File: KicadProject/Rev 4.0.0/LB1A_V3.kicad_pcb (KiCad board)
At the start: 6 copper layers, 42 x 42 mm, 187 parts, among them J601 2337019-1, J602 2337019-1, U101 STM32MP157CAA3, U201 AS4C256M16D3LC-12BCN, U401 STPMIC1xPQR, U501 S40FC004C1B2C00000, U601 LBEE59B1LV-278, U701 DF40C-70DP-0.4V(51), U702 DF40C-100DP-0.4V(51), U703 DF40C-100DP-0.4V(51), X101 32.768kHz, Y101 24MHz

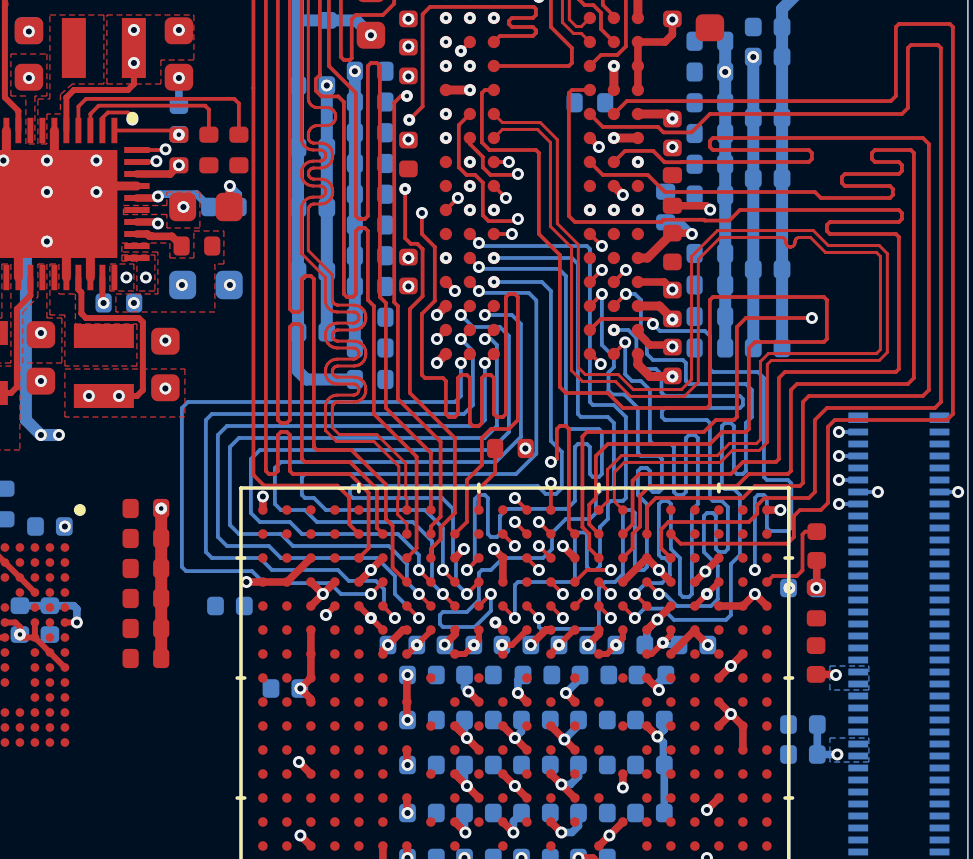
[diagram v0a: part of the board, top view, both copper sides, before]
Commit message: cleaning traces on L6 and rerouting
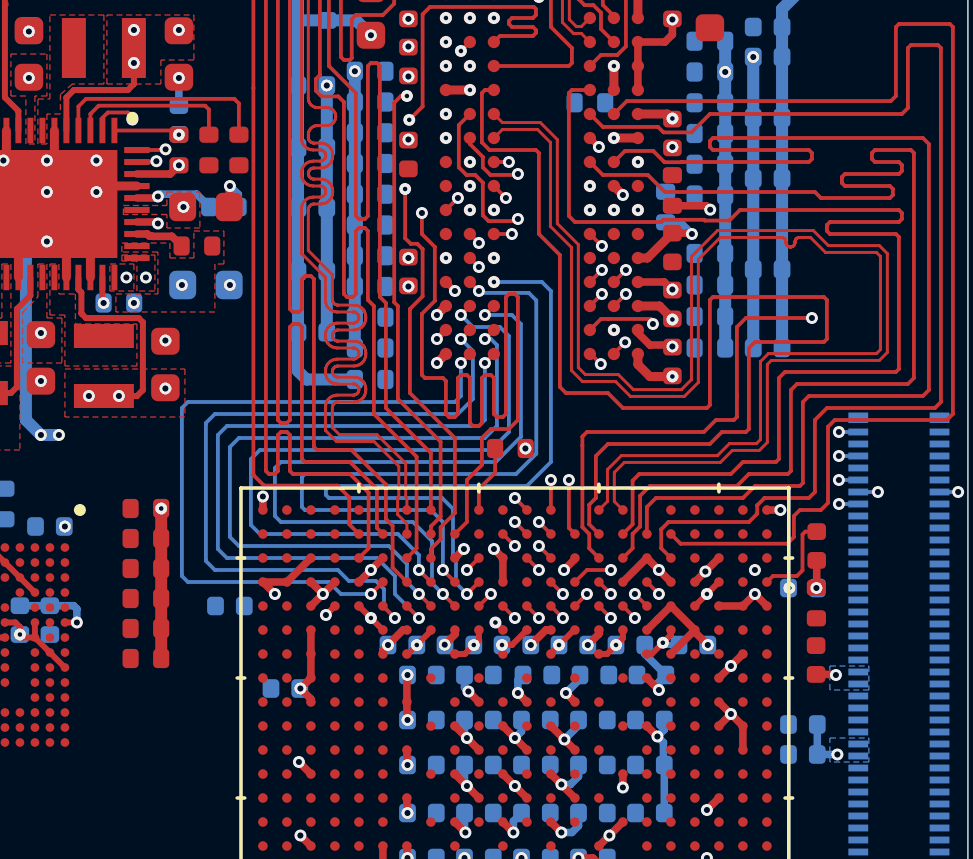
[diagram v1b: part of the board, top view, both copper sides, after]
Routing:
- net /MPU_DDR3L_Memory/DDR_BA2: track 23.5 -> 0.57 mm
- net /MPU_DDR3L_Memory/DDR_A6: track 23.4 -> 0.57 mm
- net /MPU_DDR3L_Memory/DDR_CSN: track 23.6 -> 0.99 mm
- net /MPU_DDR3L_Memory/DDR_BA0: track 23.5 -> 0.99 mm
- net /MPU_DDR3L_Memory/DDR_A4: track 23.6 -> 1.13 mm
- net /MPU_DDR3L_Memory/DDR_A1: track 23.5 -> 1.13 mm
- net /MPU_DDR3L_Memory/DDR_BA1: track 23.5 -> 1.13 mm
- net /MPU_DDR3L_Memory/DDR_A14: track 23.4 -> 1.07 mm
- net /MPU_DDR3L_Memory/DDR_A8: track 23.4 -> 1.11 mm
- net /MPU_DDR3L_Memory/DDR_A11: track 25.9 -> 10.3 mm
- net GND: track 203.9 -> 205.4 mm, vias 163 -> 162
- net /MPU_DDR3L_Memory/DDR_CLK_P: vias 1 -> 2

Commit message: some more changes
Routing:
- net /MPU_DDR3L_Memory/DDR_CLK_N: track 0.57 -> 32.7 mm
- net /MPU_DDR3L_Memory/DDR_CLK_P: track 0.57 -> 32.7 mm
- net /MPU_DDR3L_Memory/DDR_A11: track 10.3 -> 3.79 mm, vias 3 -> 2

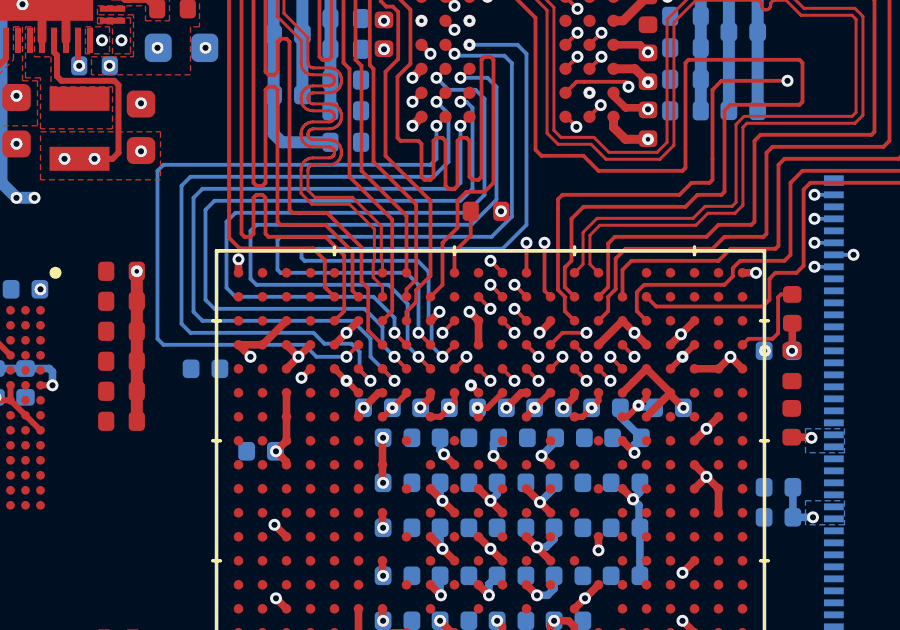
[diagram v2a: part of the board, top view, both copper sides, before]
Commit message: adjusted ground via
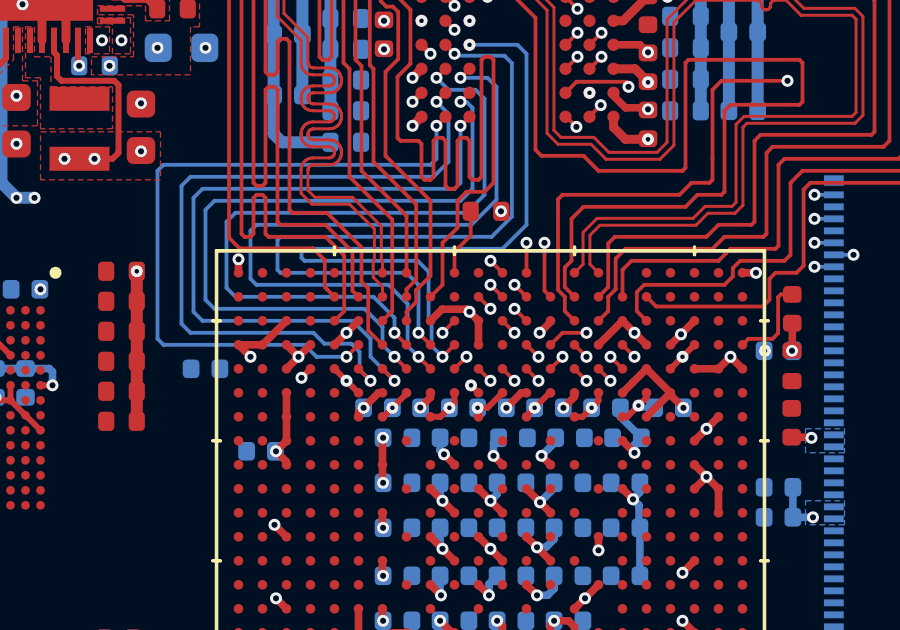
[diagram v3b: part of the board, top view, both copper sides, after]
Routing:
- net GND: track 205.4 -> 206.4 mm, vias 162 -> 161
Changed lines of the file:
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@@
     (thickness 1.2)
     (drawings 8)
-    (tracks 2430)
+    (tracks 2431)
     (zones 0)
     (modules 187)
@@
     (0 L1_Sig_Pwr.Cu mixed hide)
     (1 L2_Gnd.Cu power hide)
-    (2 L3_Sig_Pwr.Cu mixed)
-    (3 L4_Sig_Gnd.Cu mixed)
+    (2 L3_Sig_Pwr.Cu mixed hide)
+    (3 L4_Sig_Gnd.Cu mixed hide)
     (4 L5_Gnd_Pwr.Cu power hide)
     (31 L6_Sig_Pwr.Cu mixed)
@@
   (segment (start 204.280677 97.26) (end 204.41 97.389323) (width 0.254) (layer L1_Sig_Pwr.Cu) (net 1))
   (segment (start 203.15 97.26) (end 204.280677 97.26) (width 0.254) (layer L1_Sig_Pwr.Cu) (net 1))
-  (via (at 196.2 108.7) (size 0.4) (drill 0.2) (layers L1_Sig_Pwr.Cu L6_Sig_Pwr.Cu) (net 1))
-  (segment (start 195.9 109) (end 196.2 108.7) (width 0.254) (layer L1_Sig_Pwr.Cu) (net 1))
-  (segment (start 195.9 109.000001) (end 195.9 109) (width 0.254) (layer L1_Sig_Pwr.Cu) (net 1))
   (via (at 197.2 108.7) (size 0.4) (drill 0.2) (layers L1_Sig_Pwr.Cu L6_Sig_Pwr.Cu) (net 1))
   (segment (start 197.5 109) (end 197.2 108.7) (width 0.254) (layer L1_Sig_Pwr.Cu) (net 1))
@@
   (via (at 189.9 110.2) (size 0.4) (drill 0.2) (layers L1_Sig_Pwr.Cu L6_Sig_Pwr.Cu) (net 1))
   (segment (start 189.500001 109.800001) (end 189.9 110.2) (width 0.254) (layer L1_Sig_Pwr.Cu) (net 1))
+  (segment (start 197.113 108.613) (end 197.2 108.7) (width 0.254) (layer L1_Sig_Pwr.Cu) (net 1))
+  (segment (start 196.287 108.613) (end 197.113 108.613) (width 0.254) (layer L1_Sig_Pwr.Cu) (net 1))
+  (segment (start 195.9 109) (end 196.287 108.613) (width 0.254) (layer L1_Sig_Pwr.Cu) (net 1))
+  (segment (start 195.9 109.000001) (end 195.9 109) (width 0.254) (layer L1_Sig_Pwr.Cu) (net 1))
   (via (at 186.7 94.89) (size 0.4) (drill 0.15) (layers L1_Sig_Pwr.Cu L6_Sig_Pwr.Cu) (net 2))
   (segment (start 186.56 94.75) (end 186.7 94.89) (width 0.127) (layer L1_Sig_Pwr.Cu) (net 2))

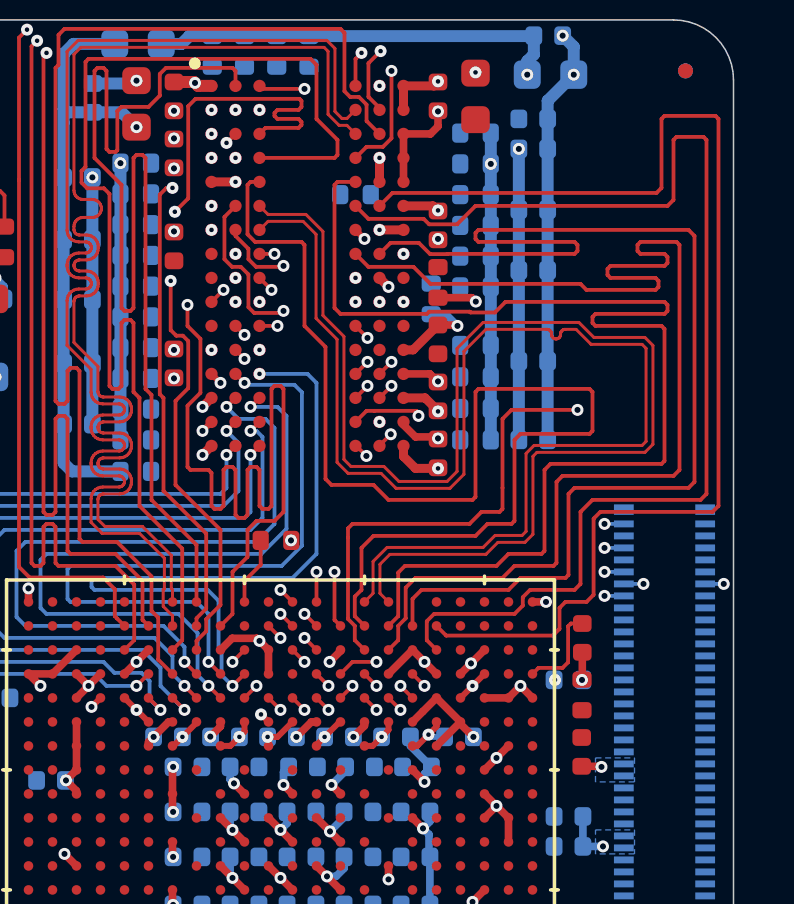
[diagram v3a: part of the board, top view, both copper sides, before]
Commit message: routed some traces
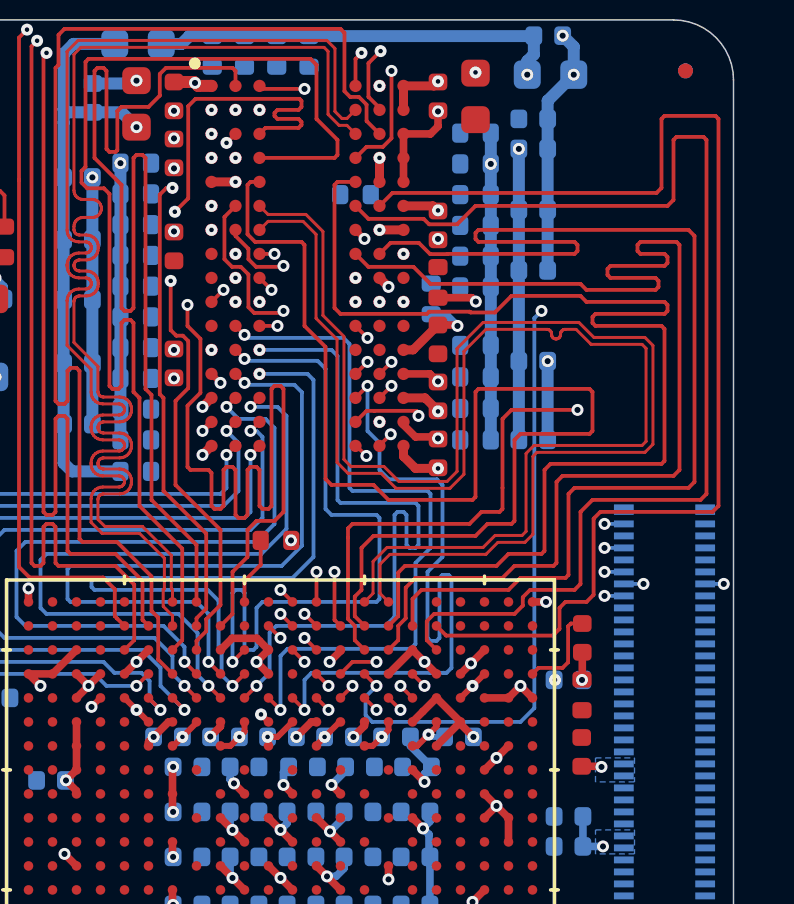
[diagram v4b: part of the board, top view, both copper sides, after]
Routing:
- net /MPU_DDR3L_Memory/DDR_CKE: track 0.57 -> 25.8 mm, vias 2 -> 3
- net /MPU_DDR3L_Memory/DDR_BA2: track 0.57 -> 23.8 mm
- net /MPU_DDR3L_Memory/DDR_CSN: track 0.99 -> 23.9 mm
- net /MPU_DDR3L_Memory/DDR_BA0: track 0.99 -> 23.7 mm
- net /MPU_DDR3L_Memory/DDR_A1: track 1.13 -> 23.7 mm
- net GND: track 206.4 -> 203.7 mm, vias 161 -> 162
- net /MPU_DDR3L_Memory/DDR_CLK_N: track 32.7 -> 31.3 mm
- net /MPU_DDR3L_Memory/DDR_CLK_P: track 32.7 -> 32.0 mm

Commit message: some more traces done
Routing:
- net /MPU_DDR3L_Memory/DDR_A12: track 1.13 -> 23.8 mm

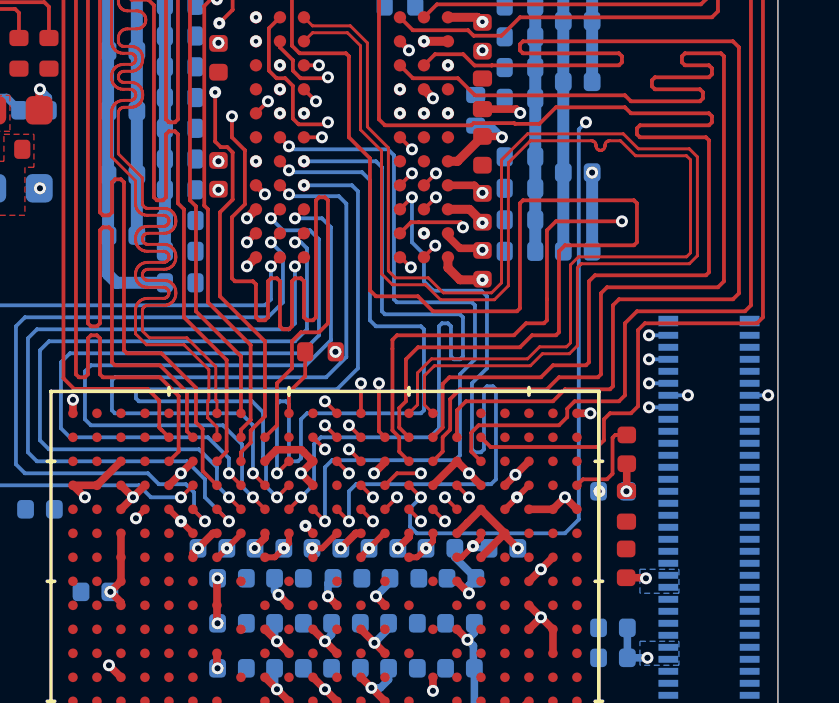
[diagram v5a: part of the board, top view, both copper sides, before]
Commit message: some more traces
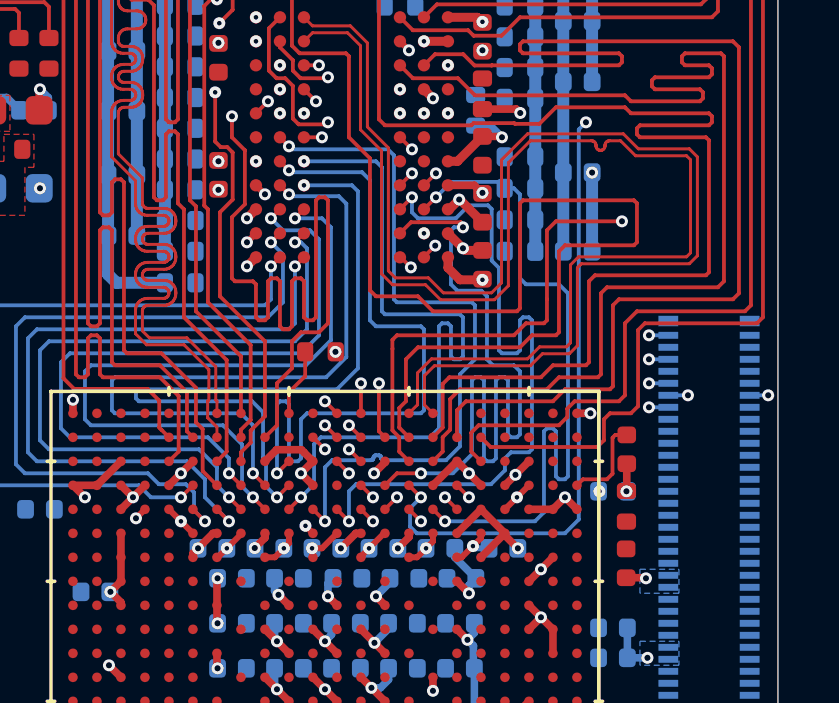
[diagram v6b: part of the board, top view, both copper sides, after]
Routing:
- net /MPU_DDR3L_Memory/DDR_A14: track 1.07 -> 23.7 mm
- net /MPU_DDR3L_Memory/DDR_A10: track 1.13 -> 23.7 mm
- net /MPU_DDR3L_Memory/DDR_A4: track 1.13 -> 23.6 mm
- net /MPU_DDR3L_Memory/DDR_A11: track 3.79 -> 26.2 mm

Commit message: ram complete. Pull up resistors pending
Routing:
- net /MPU_DDR3L_Memory/DDR_A6: track 0.57 -> 23.8 mm
- net /MPU_DDR3L_Memory/DDR_A8: track 1.11 -> 23.9 mm
- net /MPU_DDR3L_Memory/DDR_BA1: track 1.13 -> 23.8 mm
